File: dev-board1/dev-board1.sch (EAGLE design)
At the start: 172 parts, among them IC1 MSP432E401, IC10 CC3120MOD, IC2 MT48LC16M16A2, IC3 SIM800C, IC5 TPD3E001DRL, IC6 TPD3E001DRL, IC7 TPD3E001DRL, IC8 BQ25601, IC9 TPS62082, J1 MAGJACK-RJMG16XXX-8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

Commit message: getting closer...
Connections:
- net N$66: now also IC10.FLASH_CLK, JP12.4; no longer IC10.!FLASH_CS, JP12.2
- net N$69: now also IC10.!FLASH_CS; no longer IC10.FLASH_CLK
- net N$70: now also JP12.5; no longer JP12.4
- net N$71: now also JP12.2; no longer JP12.5
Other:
- moved on the sheet: JP12
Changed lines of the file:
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@@
 <instance part="JP10" gate="G$1" x="157.48" y="-111.76" rot="R180"/>
 <instance part="JP11" gate="G$1" x="160.02" y="-124.46" rot="R180"/>
-<instance part="JP12" gate="G$1" x="96.52" y="-93.98"/>
-<instance part="GND76" gate="1" x="104.14" y="-101.6"/>
+<instance part="JP12" gate="G$1" x="86.36" y="-109.22"/>
+<instance part="GND76" gate="1" x="93.98" y="-116.84"/>
 <instance part="JP6" gate="G$1" x="-215.9" y="213.36"/>
 <instance part="GND77" gate="1" x="-205.74" y="205.74"/>
@@
 </segment>
 </net>
-<net name="N$66" class="0">
-<segment>
-<pinref part="IC10" gate="G$1" pin="!FLASH_CS"/>
-<pinref part="JP12" gate="G$1" pin="2"/>
-</segment>
-</net>
-<net name="N$69" class="0">
-<segment>
-<pinref part="IC10" gate="G$1" pin="FLASH_CLK"/>
-<pinref part="JP12" gate="G$1" pin="3"/>
-</segment>
-</net>
-<net name="N$70" class="0">
-<segment>
-<pinref part="IC10" gate="G$1" pin="FLASH_MOSI"/>
-<pinref part="JP12" gate="G$1" pin="4"/>
-</segment>
-</net>
-<net name="N$71" class="0">
-<segment>
-<pinref part="IC10" gate="G$1" pin="FLASH_MISO"/>
-<pinref part="JP12" gate="G$1" pin="5"/>
-</segment>
-</net>
 <net name="N$80" class="0">
 <segment>
@@
 </segment>
 </net>
+<net name="N$70" class="0">
+<segment>
+<pinref part="IC10" gate="G$1" pin="FLASH_MOSI"/>
+<pinref part="JP12" gate="G$1" pin="5"/>
+<wire x1="104.14" y1="-91.44" x2="93.98" y2="-104.14" width="0.1524" layer="91"/>
+</segment>
+</net>
+<net name="N$66" class="0">
+<segment>
+<pinref part="IC10" gate="G$1" pin="FLASH_CLK"/>
+<pinref part="JP12" gate="G$1" pin="4"/>
+<wire x1="104.14" y1="-93.98" x2="93.98" y2="-106.68" width="0.1524" layer="91"/>
+</segment>
+</net>
+<net name="N$69" class="0">
+<segment>
+<pinref part="IC10" gate="G$1" pin="!FLASH_CS"/>
+<pinref part="JP12" gate="G$1" pin="3"/>
+<wire x1="104.14" y1="-96.52" x2="93.98" y2="-109.22" width="0.1524" layer="91"/>
+</segment>
+</net>
+<net name="N$71" class="0">
+<segment>
+<pinref part="IC10" gate="G$1" pin="FLASH_MISO"/>
+<pinref part="JP12" gate="G$1" pin="2"/>
+<wire x1="104.14" y1="-88.9" x2="93.98" y2="-111.76" width="0.1524" layer="91"/>
+</segment>
+</net>

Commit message: load of routing again again again
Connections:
- new net JOYC: IC1K.PK7, JP15.CENT
- new net JOYD: IC1M.PM6, JP15.DOWN
- new net JOYL: IC1M.PM5, JP15.LEFT
- new net JOYR: IC1M.PM4, JP15.RIGHT
- new net JOYU: IC1M.PM7, JP15.UP
- net GND: now also JP15.COM
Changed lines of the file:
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@@
 <part name="+3V18" library="supply1" deviceset="+3V3" device=""/>
 <part name="+3V19" library="supply1" deviceset="+3V3" device=""/>
+<part name="GND80" library="supply1" deviceset="GND" device=""/>
 </parts>
 <sheets>
@@
 <instance part="+3V18" gate="G$1" x="-358.14" y="-7.62"/>
 <instance part="+3V19" gate="G$1" x="-360.68" y="-10.16"/>
+<instance part="GND80" gate="1" x="-43.18" y="-137.16"/>
 </instances>
 <busses>
@@
 <pinref part="GND86" gate="1" pin="GND"/>
 </segment>
+<segment>
+<pinref part="JP15" gate="G$1" pin="COM"/>
+<pinref part="GND80" gate="1" pin="GND"/>
+</segment>
 </net>
 <net name="N$2" class="0">
@@
 </segment>
 </net>
+<net name="JOYU" class="0">
+<segment>
+<pinref part="JP15" gate="G$1" pin="UP"/>
+<wire x1="-43.18" y1="-129.54" x2="-50.8" y2="-129.54" width="0.1524" layer="91"/>
+<label x="-48.26" y="-129.54" size="1.778" layer="95" rot="MR0"/>
+</segment>
+<segment>
+<pinref part="IC1" gate="M" pin="PM7"/>
+<wire x1="-58.42" y1="-43.18" x2="-66.04" y2="-43.18" width="0.1524" layer="91"/>
+<label x="-63.5" y="-43.18" size="1.778" layer="95"/>
+</segment>
+</net>
+<net name="JOYD" class="0">
+<segment>
+<pinref part="JP15" gate="G$1" pin="DOWN"/>
+<wire x1="-53.34" y1="-132.08" x2="-43.18" y2="-132.08" width="0.1524" layer="91"/>
+<label x="-48.26" y="-132.08" size="1.778" layer="95" rot="MR0"/>
+</segment>
+<segment>
+<pinref part="IC1" gate="M" pin="PM6"/>
+<wire x1="-66.04" y1="-40.64" x2="-58.42" y2="-40.64" width="0.1524" layer="91"/>
+<label x="-63.5" y="-40.64" size="1.778" layer="95"/>
+</segment>
+</net>
+<net name="JOYC" class="0">
+<segment>
+<pinref part="JP15" gate="G$1" pin="CENT"/>
+<wire x1="-17.78" y1="-134.62" x2="-5.08" y2="-134.62" width="0.1524" layer="91"/>
+<label x="-12.7" y="-134.62" size="1.778" layer="95"/>
+</segment>
+<segment>
+<pinref part="IC1" gate="K" pin="PK7"/>
+<wire x1="-96.52" y1="-73.66" x2="-96.52" y2="-83.82" width="0.1524" layer="91"/>
+<label x="-93.98" y="-73.66" size="1.778" layer="95"/>
+<wire x1="-96.52" y1="-73.66" x2="-91.44" y2="-73.66" width="0.1524" layer="91"/>
+</segment>
+</net>
+<net name="JOYL" class="0">
+<segment>
+<pinref part="JP15" gate="G$1" pin="LEFT"/>
+<wire x1="-5.08" y1="-132.08" x2="-17.78" y2="-132.08" width="0.1524" layer="91"/>
+<label x="-12.7" y="-132.08" size="1.778" layer="95"/>
+</segment>
+<segment>
+<pinref part="IC1" gate="M" pin="PM5"/>
+<wire x1="-66.04" y1="-38.1" x2="-58.42" y2="-38.1" width="0.1524" layer="91"/>
+<label x="-63.5" y="-38.1" size="1.778" layer="95"/>
+</segment>
+</net>
+<net name="JOYR" class="0">
+<segment>
+<pinref part="JP15" gate="G$1" pin="RIGHT"/>
+<wire x1="-17.78" y1="-129.54" x2="-5.08" y2="-129.54" width="0.1524" layer="91"/>
+<label x="-12.7" y="-129.54" size="1.778" layer="95"/>
+</segment>
+<segment>
+<pinref part="IC1" gate="M" pin="PM4"/>
+<wire x1="-58.42" y1="-35.56" x2="-66.04" y2="-35.56" width="0.1524" layer="91"/>
+<label x="-63.5" y="-35.56" size="1.778" layer="95"/>
+</segment>
+</net>

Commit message: adding extra audio paths
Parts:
- removed C54: 10p, passives-7351:CAPACITOR0603-N
- removed C56, C57: 33p, passives-7351:CAPACITOR0603-N
- added C58, C61: 100n, passives-7351:CAPACITOR0603-N
- added C59: 2.2n, passives-7351:CAPACITOR0603-N
- added C60: 1n, passives-7351:CAPACITOR0603-N
- added C62: dnp, passives-7351:CAPACITOR0603-N
- added C63, C66: 33p, passives-7351:CAPACITOR0603-N
- added C64, C65: 10p, passives-7351:CAPACITOR0603-N
- added IC11: 4066D, 40xx:4066D
- added IC4: OPAMP-DUALU, SparkFun-AnalogIC:OPAMP-DUALU
- added JP16: (no value), TiLDA Mk4 Parts:M07
- added JP17: (no value), TiLDA Mk4 Parts:M02PTH
- added R46, R49, R50, R53, R54, R55: 10k, passives-7351:RESISTOR0603-N
- added R47, R48: 22k, passives-7351:RESISTOR0603-N
- added R51: 14.7k, passives-7351:RESISTOR0603-N
- added R52: 7.87k, passives-7351:RESISTOR0603-N
- added TP15: TP, Testpoint:TP
- C53: value 10p -> 100n
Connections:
- new net ADC: IC1D.PD7, IC4B.OUT, R50.P$2
- new net N$100: C59.1, R51.P$1, R52.P$2
- new net N$101: C61.2, IC11B.A, R53.P$2
- new net N$102: C62.2, IC11A.A, R53.P$1
- new net N$105: IC11A.C, IC11B.C, R55.P$2
- new net N$108: C52.1, C55.1, C63.2, C64.2, IC11D.B, U$1.1
- new net N$81: C63.1, C64.1, C65.2, C66.2, IC11C.B, U$1.2
- new net N$87: IC4B.-IN, R49.P$2, R50.P$1
- new net N$89: IC11C.C, IC11D.C, R54.P$1
- new net N$90: C59.2, C61.1, C62.1, IC4A.-IN, IC4A.OUT, TP15.P$1
- new net N$99: C60.2, IC4A.+IN, R51.P$2
- new net PWM: IC1F.PF3, JP17.2, R52.P$1
- new net SSI3CLK: IC1Q.PQ0, JP16.2
- new net SSI3DAT0: IC1Q.PQ2, JP16.4
- new net SSI3DAT1: IC1Q.PQ3, JP16.5
- new net SSI3DAT2: IC1F.PF4, JP16.6
- new net SSI3DAT3: IC1P.PP1, JP16.7
- new net SSI3FSS: IC1Q.PQ1, JP16.3
- net +3V3: now also C53.2, C58.1, IC11P.VDD, IC4A.V+, R48.P$1, R54.P$2
- net GND: now also C53.1, C58.2, C60.1, C65.1, C66.1, IC11P.VSS, IC4A.V-, JP16.1, JP17.1, R47.P$2, R55.P$1; no longer C54.1, C57.1
- net N$37: now also IC4B.+IN, R46.P$2, R47.P$1, R48.P$2; no longer IC1F.PF3
- net N$38: now also IC11B.B, IC11D.A; no longer C52.1, C53.2, C55.1, C56.2, U$1.1
- net N$40: now also R49.P$1
- net N$41: now also R46.P$1
- net N$42: now also IC11A.B, IC11C.A; no longer C53.1, C54.2, C56.1, C57.2, U$1.2
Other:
- note added: "connect"
- moved on the sheet: C52, C53, C55, U$1

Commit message: getting close
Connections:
- removed net N$105: IC11A.C, IC11B.C, R55.P$2
- removed net N$89: IC11C.C, IC11D.C, R54.P$1
- new net MUX_A: IC11C.C, IC11D.C, IC1N.PN1, R54.P$1
- new net MUX_B: IC11A.C, IC11B.C, IC1N.PN2, R55.P$2
- net JOYC: now also IC1N.PN0, IC1P.PP0; no longer IC1K.PK7
- net PWR_KEY: now also IC1P.PP5; no longer IC1Q.PQ4
- net SIM_STATUS: now also IC1Q.PQ4; no longer IC1P.PP5
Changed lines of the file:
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@@
 <net name="NETLIGHT" class="0">
+<segment>
+<wire x1="45.72" y1="93.98" x2="22.86" y2="93.98" width="0.1524" layer="91"/>
+<label x="22.86" y="93.98" size="1.778" layer="95"/>
+<pinref part="R35" gate="G$1" pin="P$2"/>
+</segment>
 <segment>
 <pinref part="IC1" gate="P" pin="PP4"/>
 <wire x1="-38.1" y1="-35.56" x2="-33.02" y2="-35.56" width="0.1524" layer="91"/>
 <label x="-35.56" y="-35.56" size="1.778" layer="95"/>
-</segment>
-<segment>
-<wire x1="45.72" y1="93.98" x2="22.86" y2="93.98" width="0.1524" layer="91"/>
-<label x="22.86" y="93.98" size="1.778" layer="95"/>
-<pinref part="R35" gate="G$1" pin="P$2"/>
 </segment>
 </net>
@@
 <net name="PWR_KEY" class="0">
 <segment>
-<pinref part="IC1" gate="Q" pin="PQ4"/>
-<wire x1="-38.1" y1="-60.96" x2="-30.48" y2="-60.96" width="0.1524" layer="91"/>
-<label x="-35.56" y="-60.96" size="1.778" layer="95"/>
-</segment>
-<segment>
 <pinref part="Q3" gate="G$1" pin="G"/>
 <wire x1="60.96" y1="78.74" x2="48.26" y2="78.74" width="0.1524" layer="91"/>
 <label x="43.18" y="78.74" size="1.778" layer="95"/>
 </segment>
+<segment>
+<pinref part="IC1" gate="P" pin="PP5"/>
+<wire x1="-33.02" y1="-38.1" x2="-38.1" y2="-38.1" width="0.1524" layer="91"/>
+<label x="-35.56" y="-38.1" size="1.778" layer="95"/>
+</segment>
 </net>
 <net name="SIM_STATUS" class="0">
-<segment>
-<pinref part="IC1" gate="P" pin="PP5"/>
-<wire x1="-38.1" y1="-38.1" x2="-33.02" y2="-38.1" width="0.1524" layer="91"/>
-<label x="-35.56" y="-38.1" size="1.778" layer="95"/>
-</segment>
 <segment>
 <label x="78.74" y="81.28" size="1.778" layer="95"/>
@@
 <junction x="86.36" y="81.28"/>
 <pinref part="R36" gate="G$1" pin="P$2"/>
+</segment>
+<segment>
+<pinref part="IC1" gate="Q" pin="PQ4"/>
+<wire x1="-38.1" y1="-60.96" x2="-33.02" y2="-60.96" width="0.1524" layer="91"/>
+<label x="-35.56" y="-60.96" size="1.778" layer="95"/>
 </segment>
 </net>
@@
 </segment>
 <segment>
-<pinref part="IC1" gate="K" pin="PK7"/>
-<wire x1="-96.52" y1="-73.66" x2="-96.52" y2="-83.82" width="0.1524" layer="91"/>
-<label x="-93.98" y="-73.66" size="1.778" layer="95"/>
-<wire x1="-96.52" y1="-73.66" x2="-91.44" y2="-73.66" width="0.1524" layer="91"/>
+<pinref part="IC1" gate="P" pin="PP0"/>
+<wire x1="-38.1" y1="-25.4" x2="-33.02" y2="-25.4" width="0.1524" layer="91"/>
+<label x="-35.56" y="-25.4" size="1.778" layer="95"/>
+</segment>
+<segment>
+<pinref part="IC1" gate="N" pin="PN0"/>
+<wire x1="-66.04" y1="-55.88" x2="-60.96" y2="-55.88" width="0.1524" layer="91"/>
+<label x="-63.5" y="-55.88" size="1.778" layer="95"/>
 </segment>
 </net>
@@
 </segment>
 </net>
-<net name="N$89" class="0">
+<net name="MUX_A" class="0">
 <segment>
 <pinref part="IC11" gate="D" pin="C"/>
@@
 <junction x="264.16" y="127"/>
 <junction x="264.16" y="142.24"/>
-</segment>
-</net>
-<net name="N$105" class="0">
+<label x="261.62" y="127" size="1.778" layer="95" rot="R180"/>
+</segment>
+<segment>
+<pinref part="IC1" gate="N" pin="PN1"/>
+<wire x1="-66.04" y1="-58.42" x2="-60.96" y2="-58.42" width="0.1524" layer="91"/>
+<label x="-63.5" y="-58.42" size="1.778" layer="95"/>
+</segment>
+</net>
+<net name="MUX_B" class="0">
 <segment>
 <pinref part="IC11" gate="B" pin="C"/>
@@
 <junction x="276.86" y="205.74"/>
 <wire x1="276.86" y1="205.74" x2="266.7" y2="205.74" width="0.1524" layer="91"/>
-</segment>
-</net>
+<label x="266.7" y="205.74" size="1.778" layer="95"/>
+</segment>
+<segment>
+<pinref part="IC1" gate="N" pin="PN2"/>
+<wire x1="-60.96" y1="-60.96" x2="-66.04" y2="-60.96" width="0.1524" layer="91"/>
+<label x="-63.5" y="-60.96" size="1.778" layer="95"/>
+</segment>
+</net>

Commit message: zero airwires
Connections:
- net JOYC: no longer IC1N.PN0
- net JOYD: now also IC1N.PN0; no longer IC1M.PM6
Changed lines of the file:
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@@
 </segment>
 <segment>
-<pinref part="IC1" gate="M" pin="PM6"/>
-<wire x1="-66.04" y1="-40.64" x2="-58.42" y2="-40.64" width="0.1524" layer="91"/>
-<label x="-63.5" y="-40.64" size="1.778" layer="95"/>
+<pinref part="IC1" gate="N" pin="PN0"/>
+<wire x1="-66.04" y1="-55.88" x2="-60.96" y2="-55.88" width="0.1524" layer="91"/>
+<label x="-63.5" y="-55.88" size="1.778" layer="95"/>
 </segment>
 </net>
@@
 <label x="-35.56" y="-25.4" size="1.778" layer="95"/>
 </segment>
-<segment>
-<pinref part="IC1" gate="N" pin="PN0"/>
-<wire x1="-66.04" y1="-55.88" x2="-60.96" y2="-55.88" width="0.1524" layer="91"/>
-<label x="-63.5" y="-55.88" size="1.778" layer="95"/>
-</segment>
 </net>

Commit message: finishing touches...
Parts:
- removed U3: ER-TFT024-3-OUTLINE, TiLDA Mk4 Parts:ER-TFT024-3-OUTLINE
- R45: value 0603/220k/5% -> 10k; device TiLDA Mk3 Parts:R-EU_0603K-SMALL -> passives-7351:RESISTOR0603-N
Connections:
- net VBAT_SWITCH_CONTROL: now also R45.P$1; no longer R45.2
- net VBAT_UNSWITCH: now also R45.P$2; no longer R45.1
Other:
- moved on the sheet: R45
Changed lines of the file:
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@@
 <part name="GND31" library="supply1" deviceset="GND" device=""/>
 <part name="+3V7" library="supply1" deviceset="+3V3" device=""/>
-<part name="U3" library="TiLDA Mk4 Parts" deviceset="ER-TFT024-3-OUTLINE" device=""/>
 <part name="J3" library="TiLDA Mk4 Parts" deviceset="ER-TFT024-3" device=""/>
 <part name="R17" library="passives-7351" deviceset="RESISTOR" device="0603-N" value="12"/>
@@
 <attribute name="FARNELL" value="2501103"/>
 </part>
-<part name="R45" library="TiLDA Mk3 Parts" deviceset="R-EU_" device="0603K-SMALL" value="0603/220k/5%"/>
 <part name="GND107" library="TiLDA Mk3 Parts" deviceset="GND" device=""/>
 <part name="U$1" library="SparkFun-Sensors" deviceset="MIC" device="9.7MM"/>
@@
 <part name="C53" library="passives-7351" deviceset="CAPACITOR" device="0603-N" value="100n"/>
 <part name="TP15" library="Testpoint" deviceset="TP" device=""/>
+<part name="R45" library="passives-7351" deviceset="RESISTOR" device="0603-N" value="10k"/>
 </parts>
 <sheets>
@@
 <instance part="GND31" gate="1" x="68.58" y="-78.74"/>
 <instance part="+3V7" gate="G$1" x="38.1" y="-63.5" rot="R90"/>
-<instance part="U3" gate="G$1" x="-78.74" y="248.92"/>
 <instance part="J3" gate="G$1" x="-116.84" y="248.92"/>
 <instance part="R17" gate="G$1" x="-137.16" y="312.42" rot="R180"/>
@@
 <attribute name="VALUE" x="-394.208" y="-136.906" size="1.27" layer="96"/>
 </instance>
-<instance part="R45" gate="G$1" x="-396.24" y="-147.32" rot="R270"/>
 <instance part="GND107" gate="1" x="-393.7" y="-170.18"/>
 <instance part="U$1" gate="G$1" x="335.28" y="142.24" rot="R270"/>
@@
 <instance part="C53" gate="G$1" x="256.54" y="256.54" rot="R180"/>
 <instance part="TP15" gate="G$1" x="241.3" y="228.6"/>
+<instance part="R45" gate="G$1" x="-396.24" y="-147.32" rot="R90"/>
 </instances>
 <busses>
@@
 <net name="VBAT_UNSWITCH" class="0">
 <segment>
-<wire x1="-396.24" y1="-139.7" x2="-401.32" y2="-139.7" width="0.1524" layer="91"/>
-<wire x1="-401.32" y1="-139.7" x2="-408.94" y2="-139.7" width="0.1524" layer="91"/>
+<wire x1="-396.24" y1="-139.7" x2="-419.1" y2="-139.7" width="0.1524" layer="91"/>
 <pinref part="Q6" gate="G$1" pin="S"/>
 <wire x1="-393.7" y1="-139.7" x2="-396.24" y2="-139.7" width="0.1524" layer="91"/>
-<pinref part="R45" gate="G$1" pin="1"/>
 <wire x1="-396.24" y1="-142.24" x2="-396.24" y2="-139.7" width="0.1524" layer="91"/>
 <junction x="-396.24" y="-139.7"/>
@@
 <wire x1="-238.76" y1="-114.3" x2="-419.1" y2="-114.3" width="0.1524" layer="91"/>
 <wire x1="-419.1" y1="-114.3" x2="-419.1" y2="-139.7" width="0.1524" layer="91"/>
-<wire x1="-419.1" y1="-139.7" x2="-408.94" y2="-139.7" width="0.1524" layer="91"/>
+<pinref part="R45" gate="G$1" pin="P$2"/>
 </segment>
 </net>
 <net name="VBAT_SWITCH_CONTROL" class="0">
 <segment>
-<pinref part="R45" gate="G$1" pin="2"/>
 <pinref part="Q6" gate="G$1" pin="G"/>
 <wire x1="-396.24" y1="-152.4" x2="-396.24" y2="-154.94" width="0.1524" layer="91"/>
@@
 <wire x1="-391.16" y1="-157.48" x2="-391.16" y2="-154.94" width="0.1524" layer="91"/>
 <junction x="-391.16" y="-154.94"/>
-</segment>
-</net>
+<pinref part="R45" gate="G$1" pin="P$1"/>
+</segment>
+</net>

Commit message: final prototype 1 (hopefully)
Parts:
- removed TP5, TP6: TP, Testpoint:TP
- added JP18: (no value), TiLDA Mk4 Parts:M02PTH
- added TP14: TP, Testpoint:TP
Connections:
- net ADC: now also TP14.P$1
- net N$40: now also JP18.1; no longer TP5.P$1
- net N$41: now also JP18.2; no longer TP6.P$1
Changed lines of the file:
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@@
 <part name="TP3" library="Testpoint" deviceset="TP" device=""/>
 <part name="TP4" library="Testpoint" deviceset="TP" device=""/>
-<part name="TP5" library="Testpoint" deviceset="TP" device=""/>
-<part name="TP6" library="Testpoint" deviceset="TP" device=""/>
 <part name="TP7" library="Testpoint" deviceset="TP" device=""/>
 <part name="TP8" library="Testpoint" deviceset="TP" device=""/>
@@
 <part name="TP15" library="Testpoint" deviceset="TP" device=""/>
 <part name="R45" library="passives-7351" deviceset="RESISTOR" device="0603-N" value="10k"/>
+<part name="TP14" library="Testpoint" deviceset="TP" device=""/>
+<part name="JP18" library="TiLDA Mk4 Parts" deviceset="M02" device="PTH"/>
 </parts>
 <sheets>
@@
 <instance part="TP3" gate="G$1" x="86.36" y="81.28" rot="R180"/>
 <instance part="TP4" gate="G$1" x="76.2" y="104.14"/>
-<instance part="TP5" gate="G$1" x="251.46" y="93.98"/>
-<instance part="TP6" gate="G$1" x="251.46" y="91.44" rot="R180"/>
 <instance part="TP7" gate="G$1" x="-198.12" y="104.14" rot="R90"/>
 <instance part="TP8" gate="G$1" x="-134.62" y="294.64" rot="R180"/>
@@
 <instance part="TP15" gate="G$1" x="241.3" y="228.6"/>
 <instance part="R45" gate="G$1" x="-396.24" y="-147.32" rot="R90"/>
+<instance part="TP14" gate="G$1" x="287.02" y="68.58"/>
+<instance part="JP18" gate="G$1" x="264.16" y="93.98" rot="R180"/>
 </instances>
 <busses>
@@
 <junction x="226.06" y="93.98"/>
 <wire x1="226.06" y1="93.98" x2="243.84" y2="93.98" width="0.1524" layer="91"/>
-<pinref part="TP5" gate="G$1" pin="P$1"/>
 <wire x1="243.84" y1="71.12" x2="243.84" y2="93.98" width="0.1524" layer="91"/>
 <junction x="243.84" y="93.98"/>
-<wire x1="243.84" y1="93.98" x2="251.46" y2="93.98" width="0.1524" layer="91"/>
-<wire x1="251.46" y1="93.98" x2="256.54" y2="93.98" width="0.1524" layer="91"/>
-<junction x="251.46" y="93.98"/>
+<wire x1="243.84" y1="93.98" x2="256.54" y2="93.98" width="0.1524" layer="91"/>
 <pinref part="R49" gate="G$1" pin="P$1"/>
 <wire x1="243.84" y1="71.12" x2="248.92" y2="66.04" width="0.1524" layer="91"/>
+<pinref part="JP18" gate="G$1" pin="1"/>
 </segment>
 </net>
@@
 <junction x="220.98" y="86.36"/>
 <wire x1="220.98" y1="86.36" x2="215.9" y2="86.36" width="0.1524" layer="91"/>
-<wire x1="256.54" y1="91.44" x2="251.46" y2="91.44" width="0.1524" layer="91"/>
-<wire x1="251.46" y1="91.44" x2="241.3" y2="91.44" width="0.1524" layer="91"/>
+<wire x1="256.54" y1="91.44" x2="241.3" y2="91.44" width="0.1524" layer="91"/>
 <wire x1="241.3" y1="91.44" x2="233.68" y2="91.44" width="0.1524" layer="91"/>
 <wire x1="233.68" y1="91.44" x2="233.68" y2="86.36" width="0.1524" layer="91"/>
 <wire x1="233.68" y1="86.36" x2="226.06" y2="86.36" width="0.1524" layer="91"/>
-<pinref part="TP6" gate="G$1" pin="P$1"/>
-<junction x="251.46" y="91.44"/>
 <wire x1="241.3" y1="66.04" x2="241.3" y2="91.44" width="0.1524" layer="91"/>
 <junction x="241.3" y="91.44"/>
 <pinref part="R46" gate="G$1" pin="P$1"/>
 <wire x1="248.92" y1="71.12" x2="241.3" y2="66.04" width="0.1524" layer="91"/>
+<pinref part="JP18" gate="G$1" pin="2"/>
 </segment>
 </net>
@@
 <junction x="287.02" y="68.58"/>
 <label x="287.02" y="68.58" size="1.778" layer="95"/>
+<pinref part="TP14" gate="G$1" pin="P$1"/>
 </segment>
 </net>

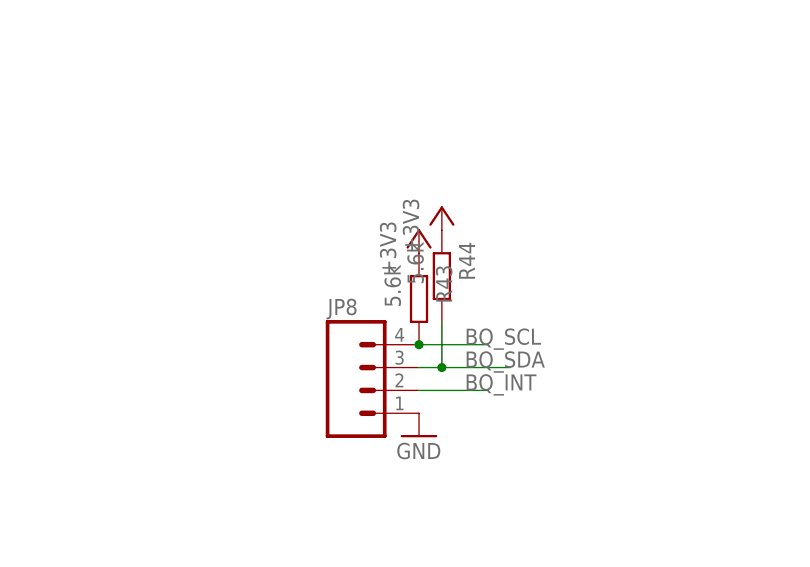
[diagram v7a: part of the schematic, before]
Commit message: adding part numbers
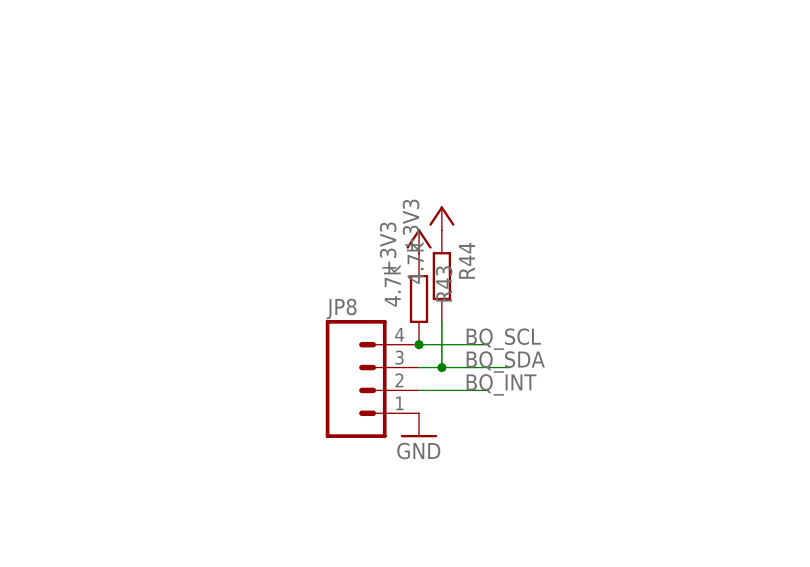
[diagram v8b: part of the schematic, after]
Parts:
- C31, C32, C51: FARNELL (none) -> 1889302
- IC11: FARNELL (none) -> 1201330
- IC2: FARNELL (none) -> 2253738
- J1: FARNELL (none) -> 1357436
- J2: FARNELL (none) -> 2213306
- L1, L2: FARNELL (none) -> 1781089
- L3: FARNELL (none) -> 2428202
- LED1: FARNELL (none) -> 2426215
- LED2, LED3, LED4, LED5: FARNELL (none) -> 2449874
- Q2: FARNELL (none) -> 2724398
- R3: FARNELL (none) -> 2447387
- R43, R44: value 5.6k -> 4.7k
- S1, S2, S3, S4, S6: FARNELL (none) -> 2320087
- U$1: FARNELL (none) -> 2396073
- U1, U2: FARNELL (none) -> 2293755
- X1: FARNELL (none) -> 2723239
- Y1: FARNELL (none) -> 2508925
